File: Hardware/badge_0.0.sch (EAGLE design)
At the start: 48 parts, among them CON1 PH_2, IC1 CP2102, J3 2X6 FEMALE, SW1 MK12C02, SW2 MK12C02, U1 SMBT2222A, U2 SMBT2222A, U4 MCP73832T-2DCI/OT

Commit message: Preliminary Neander v0.0
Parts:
- removed R14: 1k, resistor:R-EU_R0603W
- removed SJ3: SOLDERJUMPERTRACE, SparkFun-Retired:SOLDERJUMPERTRACE
- added U$12: TOUCHSWITCH, badge:TOUCHSWITCH
- U$11, U$8: value RES_ARR -> 10k
- U$6, U$7: value RES_ARR -> 100R
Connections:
- removed net N$23: LED7.C, U$7.7
- removed net N$28: R14.1, SJ3.2
- new net AUTO_DTR: J3.1, U$8.7, U1.E
- new net AUTO_RTS: J3.9, U$8.6, U2.E
- new net N$8: LED7.C, U$7.6
- net CH_PD: no longer J3.1
- net GND: now also U$12.P$1, U$2.P$1, U$3.P$1, U$4.P$1, U$5.P$1, U$6.4, U$7.4, U$8.5; no longer R14.2
- net GPIO0: now also U$5.P$2
- net GPIO15/SPI_CS: now also U$1.P$1, U$8.4; no longer SJ3.1
- net GPIO2/SDA: now also U$3.P$2
- net GPIO4: now also U$2.P$2
- net GPIO5: now also U$4.P$2
- net N$13: now also U$6.5; no longer U$6.6
- net N$15: now also U$8.3; no longer U$8.4
- net N$18: now also U$8.2; no longer U$8.3
- net N$22: now also U$7.5; no longer U$7.6
- net RESET: now also U$12.P$2; no longer J3.9
- net S_DTR: no longer U$8.6, U1.E
- net S_RTS: no longer U$8.5, U2.E
- net VCC: now also U$1.P$2
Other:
- note added: "#3.3V Voltage Regulator"
- note added: "#AUTORESET"
- note added: "#ESP-12F"
- note added: "#GPIO"
- note added: "#LCD"
- note added: "#Li-Ion Charger"
- note added: "#USB-SERIAL"
- note added: "Jumpers to be provided for USB-Serial functionalities"
- note removed: "serial"
- moved on the sheet: C1, C2, C3, C4, C5, C9, CON1, IC1, J1, J10, J2, J3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

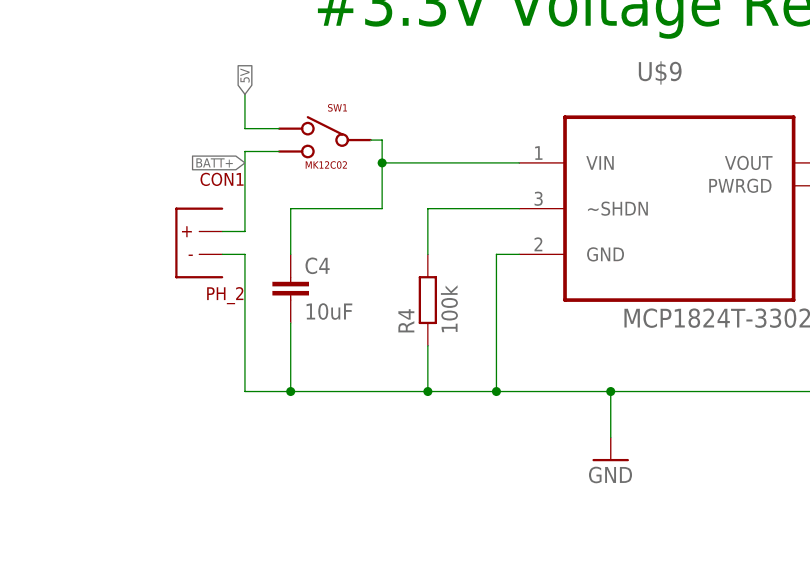
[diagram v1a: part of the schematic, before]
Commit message: Schematic: LDO !shdn is to be high, not low
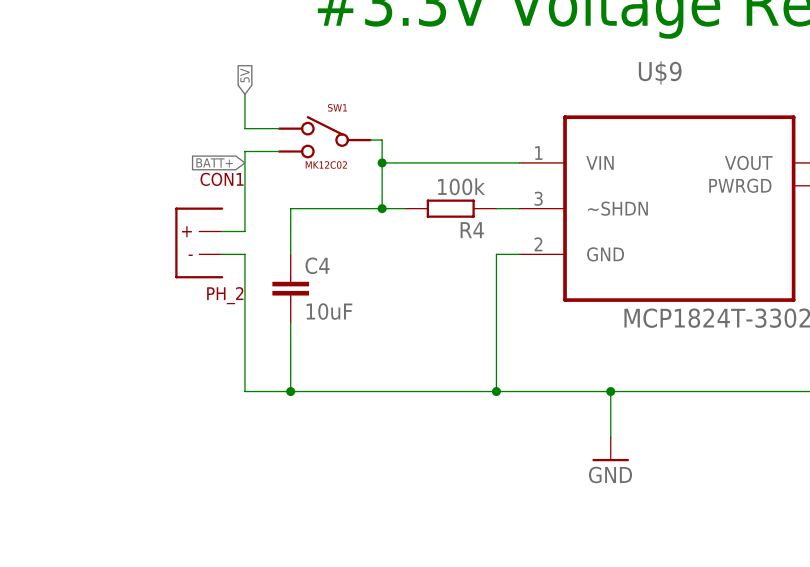
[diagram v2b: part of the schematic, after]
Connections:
- net GND: no longer R4.1
- net N$1: now also R4.2
- net N$4: now also R4.1; no longer R4.2
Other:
- moved on the sheet: R4
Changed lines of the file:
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@@
 <?xml version="1.0" encoding="utf-8"?>
 <!DOCTYPE eagle SYSTEM "eagle.dtd">
-<eagle version="7.5.0">
+<eagle version="7.1.0">
 <drawing>
 <settings>
@@
 <setting verticaltext="up"/>
 </settings>
-<grid distance="0.05" unitdist="inch" unit="inch" style="lines" multiple="1" display="no" altdistance="0.01" altunitdist="inch" altunit="inch"/>
+<grid distance="0.1" unitdist="inch" unit="inch" style="lines" multiple="1" display="no" altdistance="0.01" altunitdist="inch" altunit="inch"/>
 <layers>
 <layer number="1" name="Top" color="4" fill="1" visible="no" active="no"/>
@@
 <instance part="LED2" gate="G$1" x="320.04" y="170.18"/>
 <instance part="R2" gate="G$1" x="304.8" y="217.17" rot="R90"/>
-<instance part="R4" gate="G$1" x="251.46" y="160.02" rot="R90"/>
+<instance part="R4" gate="G$1" x="254" y="170.18" rot="R180"/>
 <instance part="C1" gate="G$1" x="264.16" y="224.79"/>
 <instance part="C2" gate="G$1" x="312.42" y="227.33"/>
@@
 <wire x1="231.14" y1="149.86" x2="236.22" y2="149.86" width="0.1524" layer="91"/>
 <junction x="236.22" y="149.86"/>
-<wire x1="236.22" y1="149.86" x2="251.46" y2="149.86" width="0.1524" layer="91"/>
-<wire x1="251.46" y1="149.86" x2="259.08" y2="149.86" width="0.1524" layer="91"/>
+<wire x1="236.22" y1="149.86" x2="259.08" y2="149.86" width="0.1524" layer="91"/>
 <wire x1="259.08" y1="149.86" x2="271.78" y2="149.86" width="0.1524" layer="91"/>
 <pinref part="U$9" gate="A" pin="GND"/>
@@
 <wire x1="259.08" y1="165.1" x2="259.08" y2="149.86" width="0.1524" layer="91"/>
 <junction x="259.08" y="149.86"/>
-<pinref part="R4" gate="G$1" pin="1"/>
-<wire x1="251.46" y1="154.94" x2="251.46" y2="149.86" width="0.1524" layer="91"/>
-<junction x="251.46" y="149.86"/>
 <pinref part="R7" gate="G$1" pin="1"/>
 <wire x1="320.04" y1="152.4" x2="320.04" y2="149.86" width="0.1524" layer="91"/>
@@
 <wire x1="246.38" y1="175.26" x2="261.62" y2="175.26" width="0.1524" layer="91"/>
 <junction x="246.38" y="175.26"/>
+<pinref part="R4" gate="G$1" pin="2"/>
+<wire x1="246.38" y1="170.18" x2="248.92" y2="170.18" width="0.1524" layer="91"/>
+<junction x="246.38" y="170.18"/>
 </segment>
 </net>
@@
 <wire x1="83.82" y1="48.26" x2="78.74" y2="48.26" width="0.1524" layer="91"/>
 <label x="78.74" y="48.26" size="1.016" layer="95" rot="R180" xref="yes"/>
-</segment>
-</net>
-<net name="N$4" class="0">
-<segment>
-<pinref part="U$9" gate="A" pin="~SHDN"/>
-<pinref part="R4" gate="G$1" pin="2"/>
-<wire x1="261.62" y1="170.18" x2="251.46" y2="170.18" width="0.1524" layer="91"/>
-<wire x1="251.46" y1="170.18" x2="251.46" y2="165.1" width="0.1524" layer="91"/>
 </segment>
 </net>
@@
 </segment>
 </net>
+<net name="N$4" class="0">
+<segment>
+<pinref part="R4" gate="G$1" pin="1"/>
+<pinref part="U$9" gate="A" pin="~SHDN"/>
+<wire x1="259.08" y1="170.18" x2="261.62" y2="170.18" width="0.1524" layer="91"/>
+</segment>
+</net>

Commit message: Fixed the files places
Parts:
- removed R3, R5: 12K, resistor:R-EU_R0603W
- removed R4: 100k, resistor:R-EU_R0603W
- removed U1, U2: SMBT2222A, badge:SMBT2222A
- added JP1: (no value), pinhead:PINHD-1X2
- added U$13: PEMH9,115, LYS_special:PEMH9,115
- J3: device SparkFun-Connectors:M06X2PTH_FEMALE -> adafruit:PINHD-2X4
- SJ1: value SOLDERJUMPERTRACE -> (none); device SparkFun-Retired:SOLDERJUMPERTRACE -> jumper:SJ
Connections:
- net N$17 renamed S_SUSP
- removed net LCD_RST: C9.1, LCD1./RES, R5.2
- removed net N$15: U$8.3, U1.B
- removed net N$16: IC1.!SUSPEND, J1.2
- removed net N$18: U$8.2, U2.B
- removed net N$19: IC1.!RST, J1.1
- new net LCD_RESET: LCD1./RES, SJ1.2, U$8.7
- net 5V: now also J1.1, R2.2; no longer J3.7, J3.8, LED1.A
- net AUTO_DTR: now also U$13.B2, U$13.E1; no longer U$8.7, U1.E
- net AUTO_RTS: now also J3.7, U$13.B1, U$13.E2; no longer J3.9, U$8.6, U2.E
- net GND: now also J1.2, JP1.1; no longer IC1.GND@M, J3.11, J3.12
- net GPIO0: now also U$13.C1; no longer U1.C
- net N$1: now also U$9.~SHDN; no longer R4.2
- net N$10: now also LED1.C; no longer R2.1
- net N$3: now also U$8.8; no longer R3.1
- net N$4: now also LED1.A, R2.1; no longer R4.1, U$9.~SHDN
- net N$5: now also IC1.GND@M; no longer SJ1.1, U$11.1, U$11.2, U$11.3, U$11.4
- net N$9: now also C9.1, LCD1.VOUT; no longer LED1.C, R2.2
- net RESET: now also SJ1.1, U$13.C2, U$8.6; no longer U$11.5, U2.C
- net S_RTS: now also J3.8; no longer J3.10
- net VCC: now also JP1.2, U$11.1, U$11.2, U$11.3, U$11.4, U$8.1, U$8.2, U$8.3; no longer R3.2, R5.1, SJ1.2
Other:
- moved on the sheet: C9, J1, J10, J8, LCD1, LED1, R2, U$8, U6

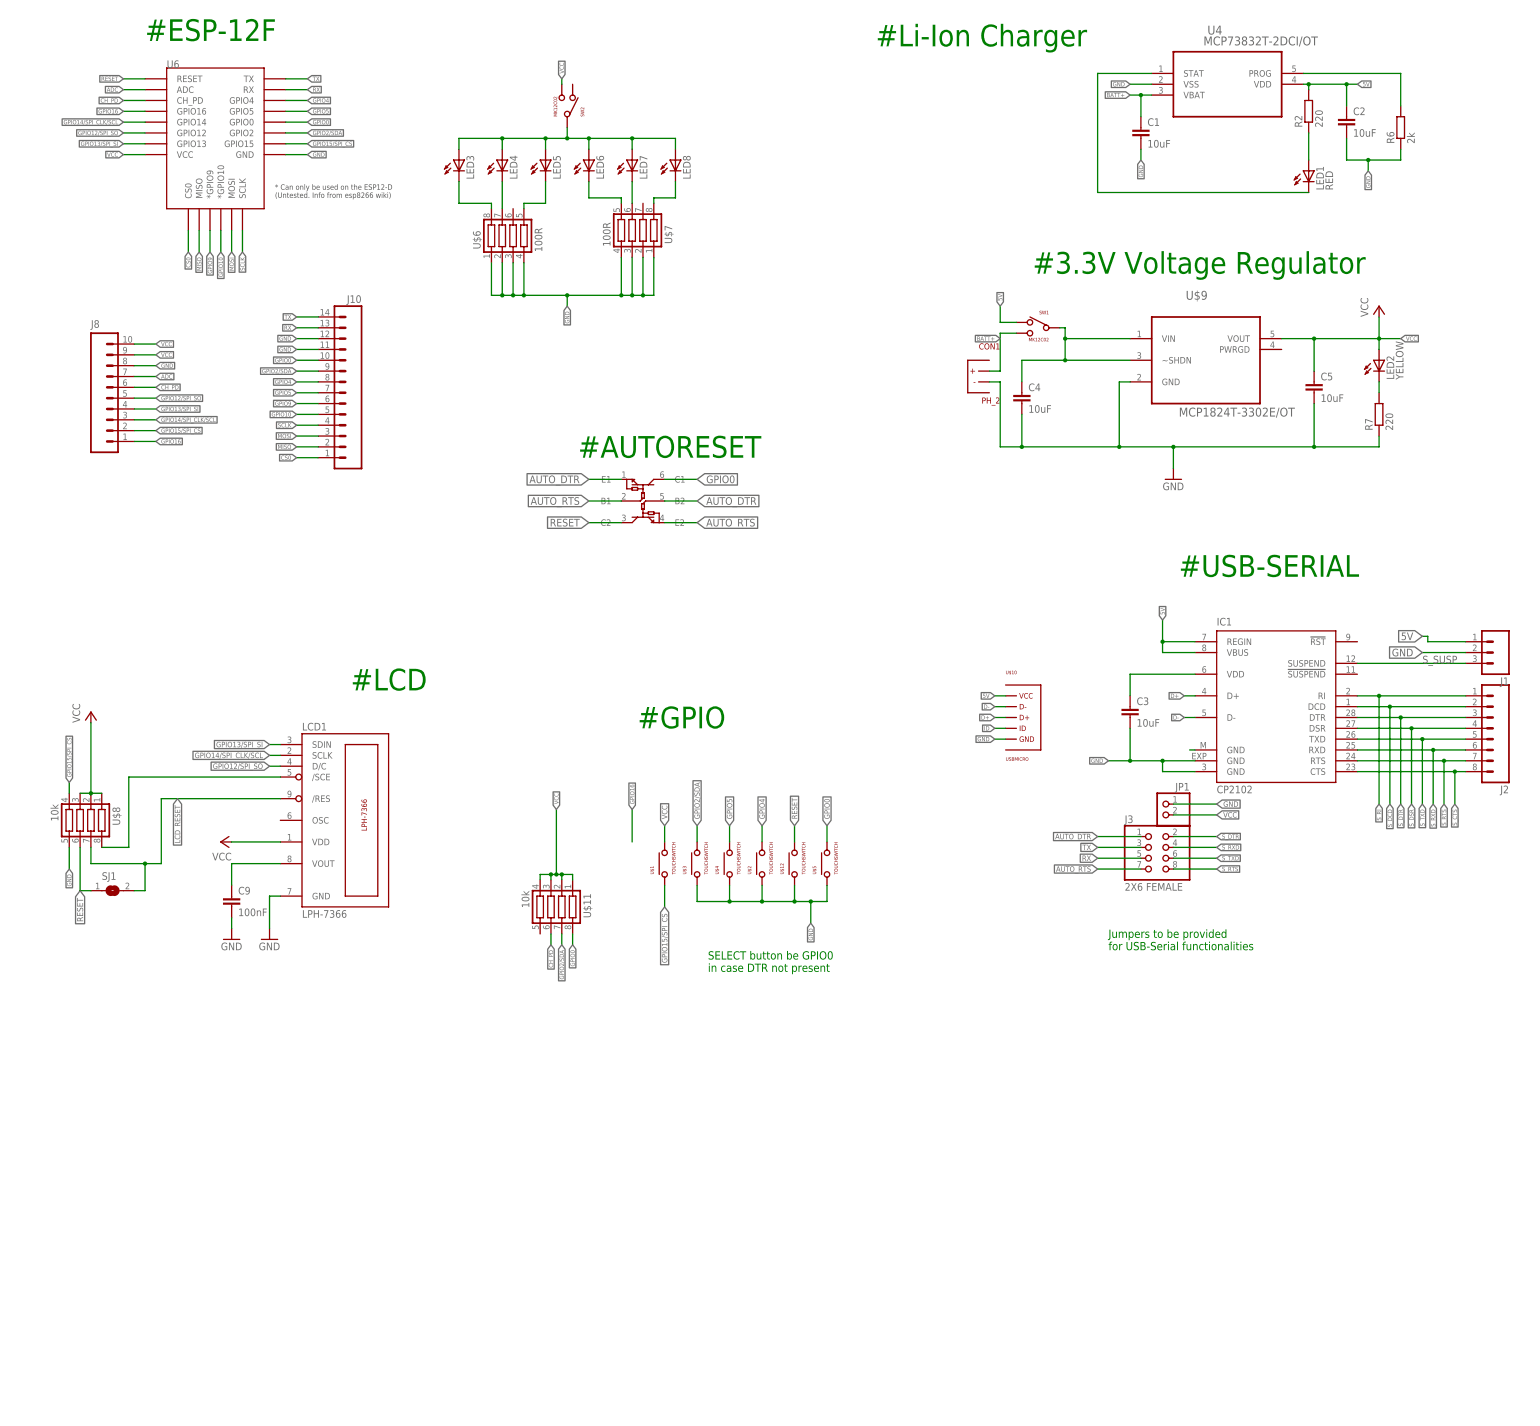
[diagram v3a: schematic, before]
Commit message: Moved power LED, sharing the r-net for the backlight
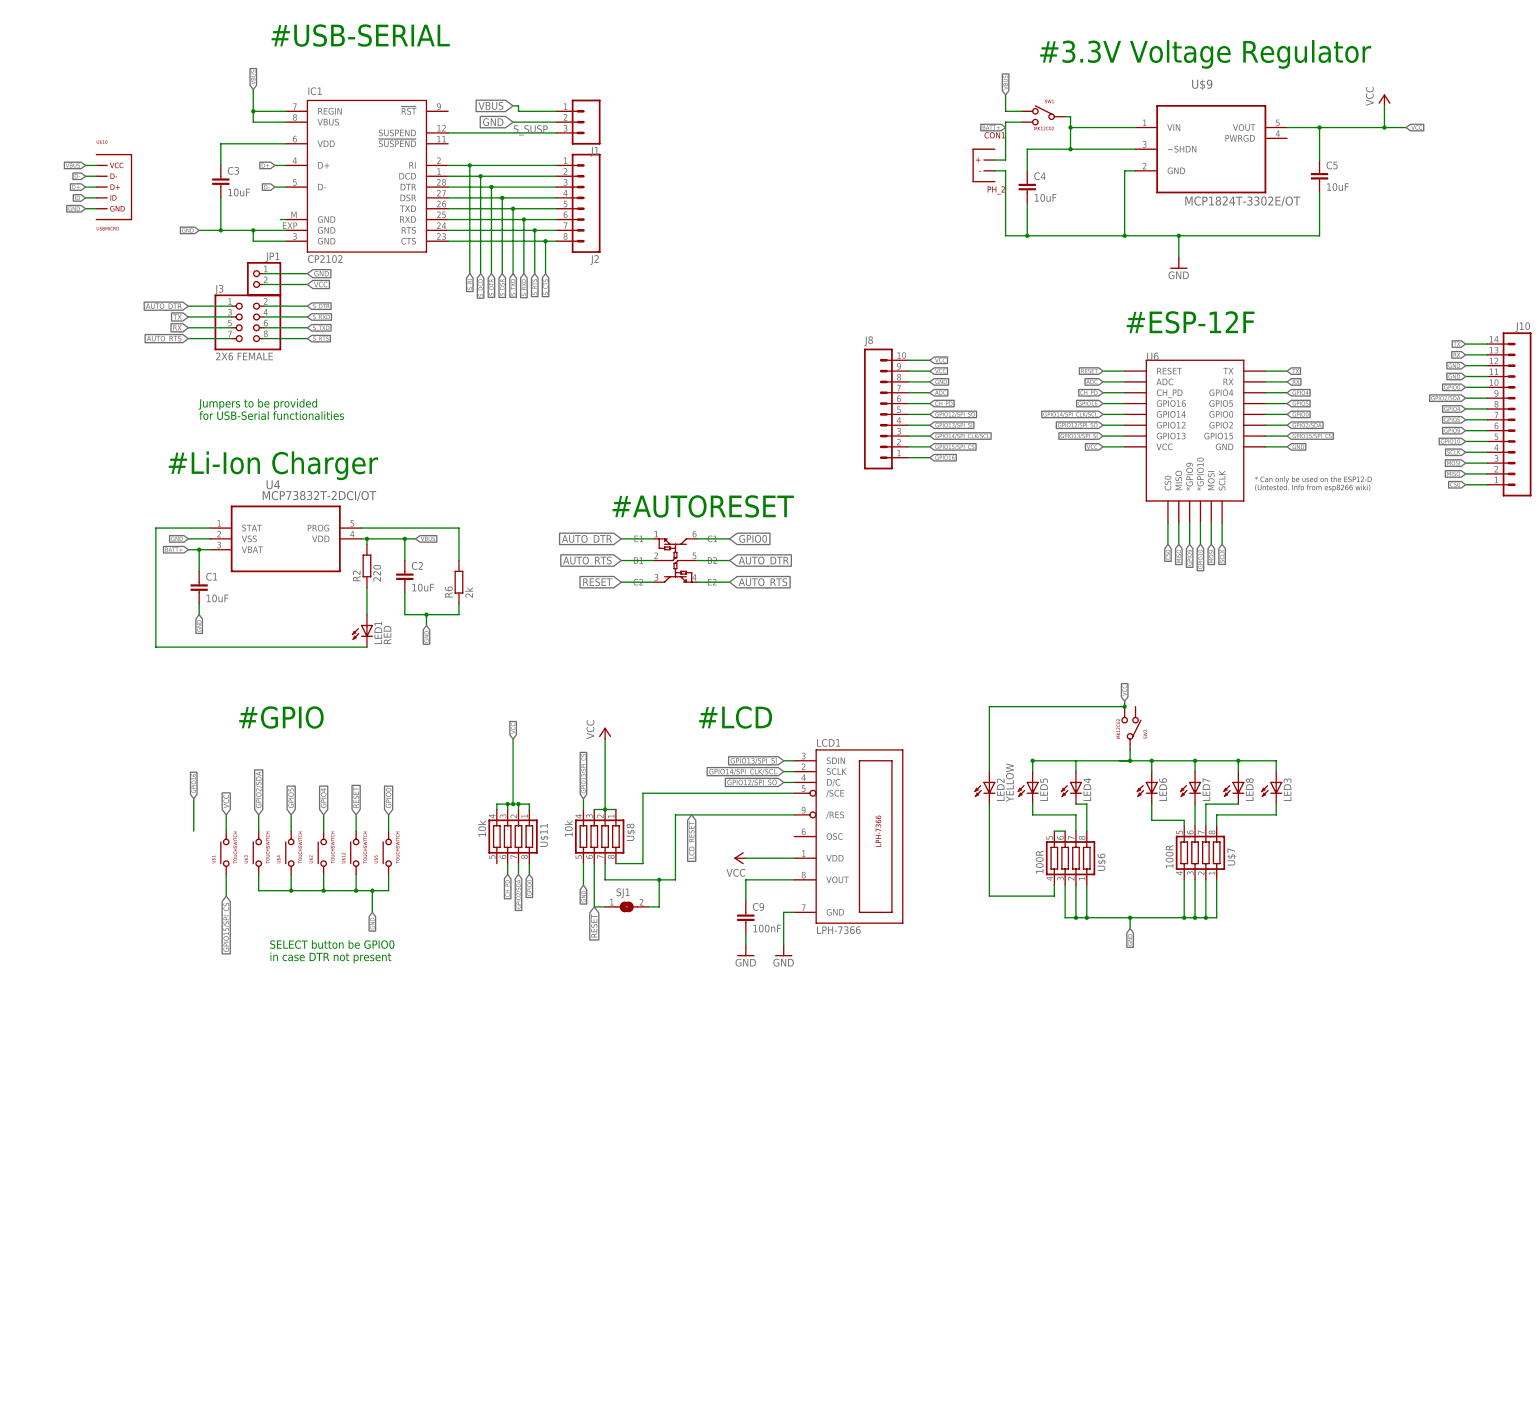
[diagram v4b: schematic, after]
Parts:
- removed R7: 220, resistor:R-EU_R0603W
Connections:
- net 5V renamed VBUS
- removed net N$24: LED8.C, U$7.8
- removed net N$7 (its old number): LED2.C, R7.2
- new net N$14: LED3.C, U$7.8
- new net N$15: LED2.C, U$6.4
- new net N$8: LED8.C, U$7.7
- net GND: no longer R7.1, U$6.4
- net N$11: now also U$6.5, U$6.6; no longer LED3.C, U$6.8
- net N$12: now also U$6.8; no longer U$6.7
- net N$13: now also U$6.7; no longer U$6.5
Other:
- moved on the sheet: C1, C2, C3, C4, C5, C9, CON1, IC1, J1, J10, J2, J3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
